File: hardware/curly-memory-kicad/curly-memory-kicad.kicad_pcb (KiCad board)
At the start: 4 copper layers, 30 x 100 mm, 84 parts, among them J101 Conn_01x06, J102 Conn_01x05, J103 Conn_01x05, J104 Conn_01x05, J105 Conn_01x05, J106 Conn_01x05, J401 Conn_02x05_Odd_Even, U101 MCP3008-I/SL, U102 ESP32-WROOM-32, U103 MCP4822-E/SN, U104 MCP4822-E/SN, U105 MCP42010-E/SL, U106 MCP42010-E/SL, U201 MCP6004, U301 MCP6004, U401 NCP1117-5.0_SOT223, U402 NCP1117-3.3_SOT223

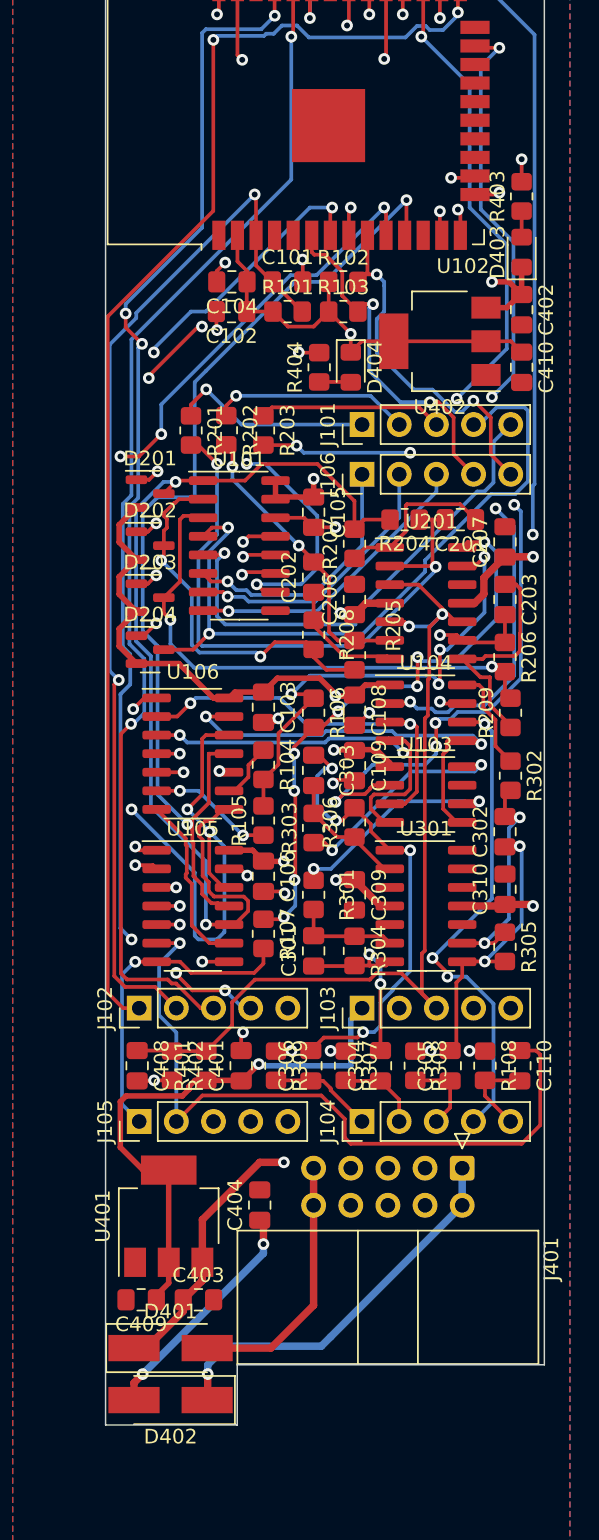
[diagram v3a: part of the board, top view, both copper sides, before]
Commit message: silkscreen lined up lovely
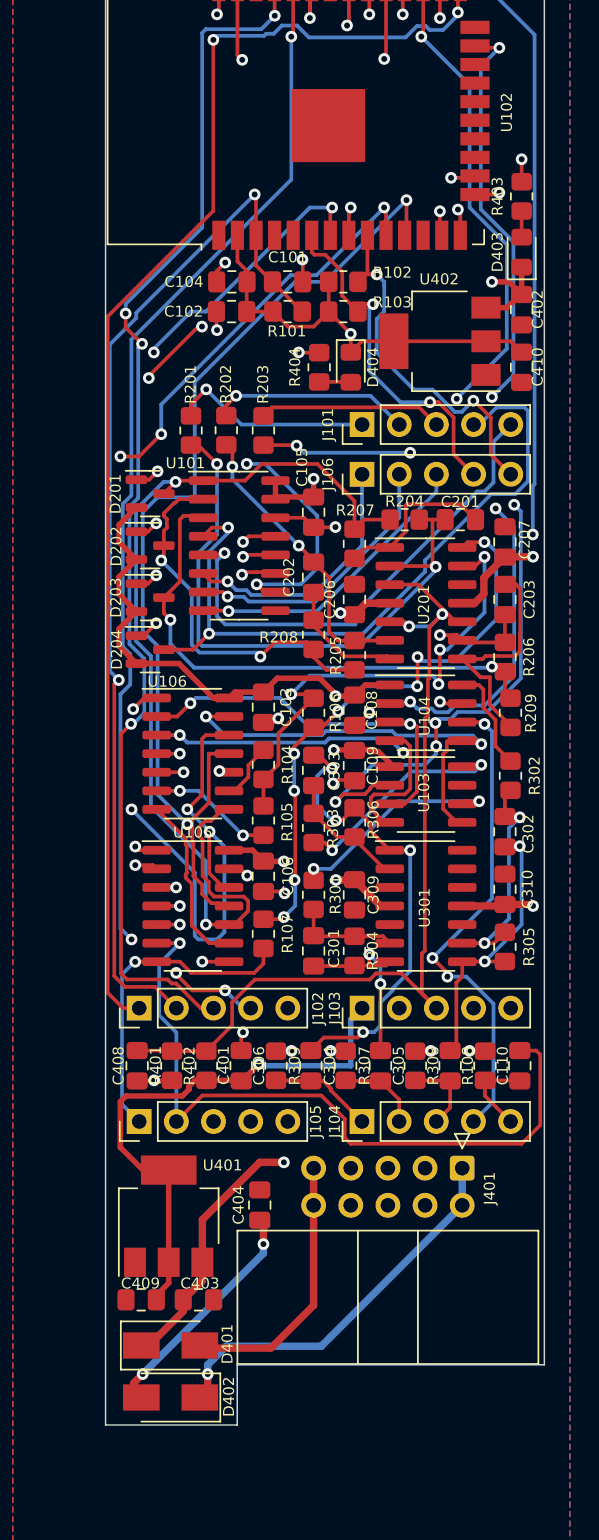
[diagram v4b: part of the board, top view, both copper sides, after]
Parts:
- D401, D402: footprint Diode_SMD:D_SMA_Handsoldering -> Diode_SMD:D_SMA
- moved D401 0.18 mm to (4.45, 94.6)
- moved D402 0.18 mm to (4.45, 98.1)

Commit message: all hardware finished
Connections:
- net Net-(J103-Pad4) renamed /IO_32
- net Net-(J103-Pad5) renamed /IO_21
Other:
- board text added: "rfe"
- board text added: "ric from ealing curly memory main board Issue A"
- board text added: "{dblquote}I would love it{dblquote} Kevin"
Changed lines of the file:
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@@
   (net 24 "Net-(D401-Pad2)")
   (net 25 "Net-(D402-Pad1)")
-  (net 26 "Net-(J103-Pad4)")
+  (net 26 "/IO_32")
   (net 27 "V_OFFSET")
   (net 28 "/LEDS")
@@
   (net 83 "Net-(D403-Pad2)")
   (net 84 "Net-(D404-Pad2)")
-  (net 85 "Net-(J103-Pad5)")
+  (net 85 "/IO_21")
   (footprint "Package_SO:SOIC-14_3.9x8.7mm_P1.27mm" (layer "F.Cu")
     (at 21.909 64.516)
@@
       (net 27 "V_OFFSET") (pinfunction "Pin_3") (pintype "passive"))
     (pad "4" thru_hole oval locked (at 0 7.62 90) (size 1.7 1.7) (drill 1) (layers *.Cu *.Mask)
-      (net 26 "Net-(J103-Pad4)") (pinfunction "Pin_4") (pintype "passive"))
+      (net 26 "/IO_32") (pinfunction "Pin_4") (pintype "passive"))
     (pad "5" thru_hole oval locked (at 0 10.16 90) (size 1.7 1.7) (drill 1) (layers *.Cu *.Mask)
-      (net 85 "Net-(J103-Pad5)") (pinfunction "Pin_5") (pintype "passive"))
+      (net 85 "/IO_21") (pinfunction "Pin_5") (pintype "passive"))
     (model "${KICAD6_3DMODEL_DIR}/Connector_PinHeader_2.54mm.3dshapes/PinHeader_1x05_P2.54mm_Vertical.wrl"
       (offset (xyz 0 0 0))
@@
       (net 28 "/LEDS") (pinfunction "IO35") (pintype "input"))
     (pad "8" smd rect locked (at -8.5 0.635 90) (size 2 0.9) (layers "F.Cu" "F.Paste" "F.Mask")
-      (net 26 "Net-(J103-Pad4)") (pinfunction "IO32") (pintype "bidirectional"))
+      (net 26 "/IO_32") (pinfunction "IO32") (pintype "bidirectional"))
     (pad "9" smd rect locked (at -8.5 1.905 90) (size 2 0.9) (layers "F.Cu" "F.Paste" "F.Mask")
       (net 51 "/SW_1") (pinfunction "IO33") (pintype "bidirectional"))
@@
       (net 76 "unconnected-(U102-Pad32)") (pinfunction "NC") (pintype "no_connect"))
     (pad "33" smd rect locked (at 8.5 -1.905 90) (size 2 0.9) (layers "F.Cu" "F.Paste" "F.Mask")
-      (net 85 "Net-(J103-Pad5)") (pinfunction "IO21") (pintype "bidirectional"))
+      (net 85 "/IO_21") (pinfunction "IO21") (pintype "bidirectional"))
     (pad "34" smd rect locked (at 8.5 -3.175 90) (size 2 0.9) (layers "F.Cu" "F.Paste" "F.Mask")
       (net 39 "/PROG_RX") (pinfunction "RXD0/IO3") (pintype "bidirectional"))
@@
   (gr_line (start 0 0) (end 30 0) (layer "Edge.Cuts") (width 0.1))
   (gr_line (start 0 100) (end 9 100) (layer "Edge.Cuts") (width 0.1))
+  (gr_text "ric from ealing\ncurly memory\nmain board\nIssue A" (at 20 89.9414) (layer "B.SilkS")
+    (effects (font (size 1 1) (thickness 0.15)) (justify mirror))
+  )
+  (gr_text "{dblquote}I would love it{dblquote}\nKevin" (at 3.81 10.8712 90) (layer "B.SilkS")
+    (effects (font (size 1 1) (thickness 0.15)) (justify mirror))
+  )
+  (gr_text "rfe" (at 20 94.1578) (layer "B.Mask")
+    (effects (font (size 1 1) (thickness 0.15)) (justify mirror))
+  )
   (segment (start 3.389511 70.049511) (end 1.33615 70.049511) (width 0.254) (layer "F.Cu") (net 1))
   (segment (start 10.287 20.7225) (end 10.287 18.66) (width 0.254) (layer "F.Cu") (net 1))
@@
       )
     )
+  )
+  (zone (net 0) (net_name "") (layers "F.Cu" "In1.Cu" "In2.Cu" "B.Cu") (hatch edge 0.508)
+    (connect_pads (clearance 0))
+    (min_thickness 0.254)
+    (keepout (tracks not_allowed) (vias not_allowed) (pads not_allowed ) (copperpour not_allowed) (footprints allowed))
+    (fill (thermal_gap 0.508) (thermal_bridge_width 0.508))
+    (polygon
+      (pts
+        (xy 6.35 17.145)
+        (xy 0 17.145)
+        (xy 0 0)
+        (xy 6.35 0)
+      )
+    )

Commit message: gerbers genearted and mf/mfpn added for main board for build
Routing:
- net /SPI3_CS_0: track 52.5 -> 56.3 mm
- net /SPI2_CS_2: track 59.1 -> 62.2 mm
- net /SPI2_MOSI: track 81.7 -> 80.0 mm
- net GND: vias 29 -> 53
